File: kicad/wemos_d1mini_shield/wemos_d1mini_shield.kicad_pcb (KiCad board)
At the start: 2 copper layers, 29 parts, among them U1 WeMosD1Mini, U11 74LS125

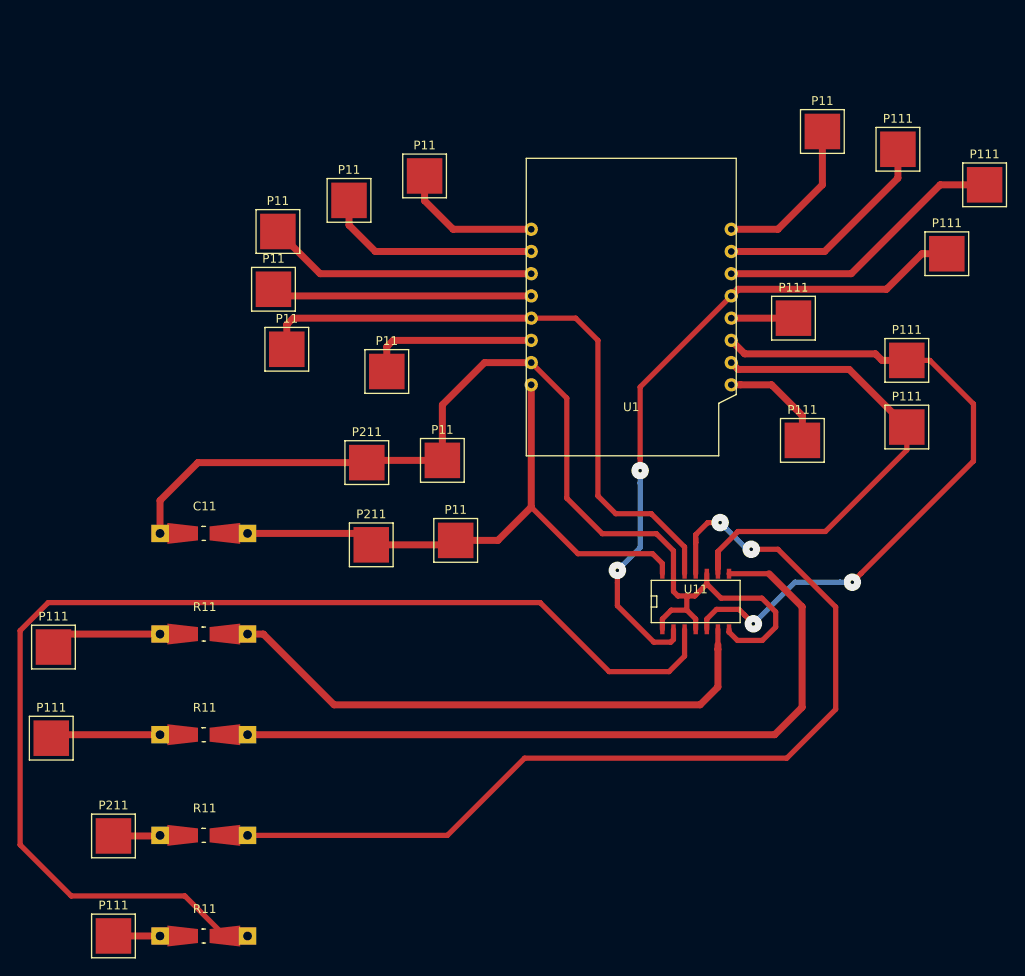
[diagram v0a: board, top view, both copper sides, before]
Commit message: kicad: simplify schematic and begin of routage (WIP)
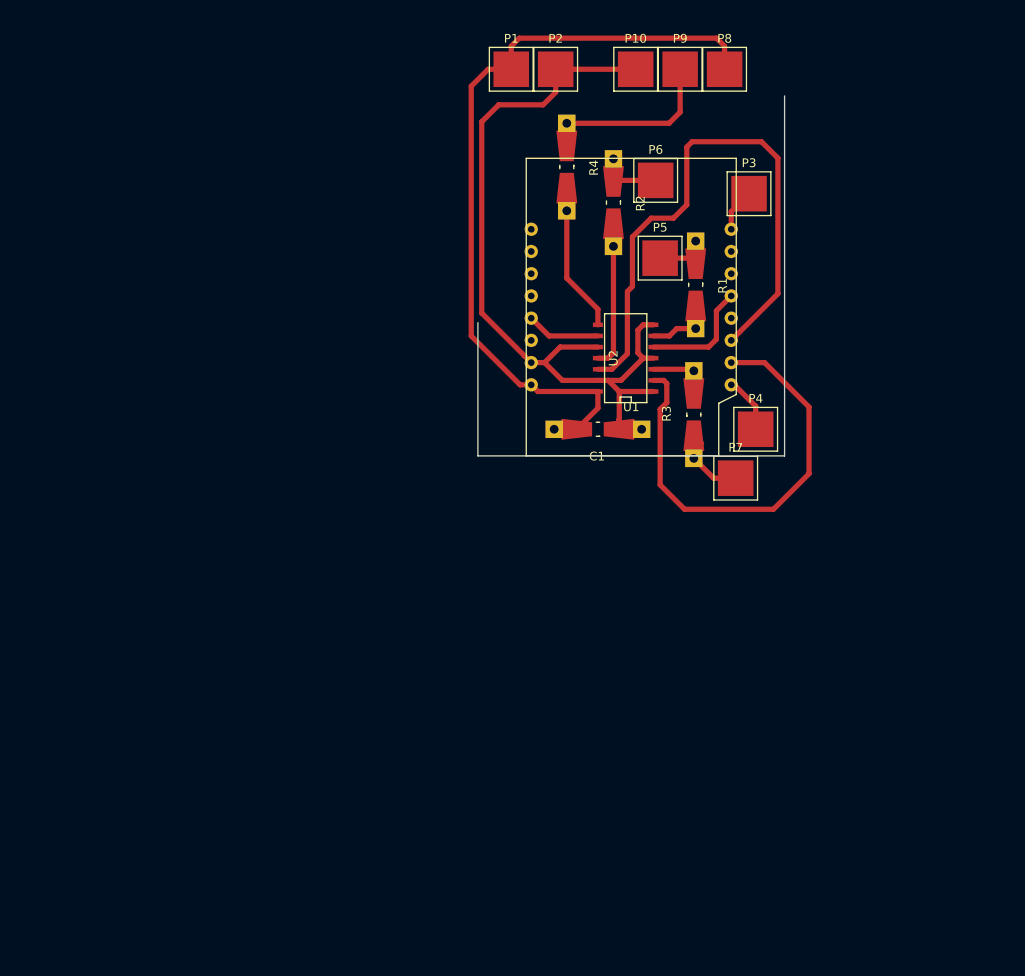
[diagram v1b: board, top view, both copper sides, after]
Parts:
- removed C11: C, Resistors_Universal:Resistor_SMD+THTuniversal_0805to1206_RM10_HandSoldering
- removed P11 (x9), P111 (x10), P211 (x3): ~, SMD_Packages:1Pin
- removed R11 (x4): R, Resistors_Universal:Resistor_SMD+THTuniversal_0805to1206_RM10_HandSoldering
- removed U11: 74LS125, SMD_Packages:SOIC-14_N
- added C1: C, Resistors_Universal:Resistor_SMD+THTuniversal_0805to1206_RM10_HandSoldering, F.Cu at (144.8, 111.8)
- added P1: ~, SMD_Packages:1Pin, F.Cu at (134.9, 70.6)
- added P10: ~, SMD_Packages:1Pin, F.Cu at (149.1, 70.6)
- added P2: ~, SMD_Packages:1Pin, F.Cu at (140.0, 70.6)
- added P3: ~, SMD_Packages:1Pin, F.Cu at (162.1, 84.8)
- added P4: ~, SMD_Packages:1Pin, F.Cu at (162.8, 111.8)
- added P5: ~, SMD_Packages:1Pin, F.Cu at (151.9, 92.2)
- added P6: ~, SMD_Packages:1Pin, F.Cu at (151.4, 83.3)
- added P7: ~, SMD_Packages:1Pin, F.Cu at (160.5, 117.3)
- added P8: ~, SMD_Packages:1Pin, F.Cu at (159.3, 70.6)
- added P9: ~, SMD_Packages:1Pin, F.Cu at (154.2, 70.6)
- added R1: R, Resistors_Universal:Resistor_SMD+THTuniversal_0805to1206_RM10_HandSoldering, F.Cu at (156.0, 95.2)
- added R2: R, Resistors_Universal:Resistor_SMD+THTuniversal_0805to1206_RM10_HandSoldering, F.Cu at (146.6, 85.9)
- added R3: R, Resistors_Universal:Resistor_SMD+THTuniversal_0805to1206_RM10_HandSoldering, F.Cu at (155.7, 110.1)
- added R4: R, Resistors_Universal:Resistor_SMD+THTuniversal_0805to1206_RM10_HandSoldering, F.Cu at (141.2, 81.8)
- added U2: 74LS125, SMD_Packages:SOIC-14_N, F.Cu at (147.8, 103.6)
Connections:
- U1 pad 1: Net-(P3-Pad1) (its old number) -> (no net)
- U1 pad 12: Net-(P12-Pad1) -> (no net)
- U1 pad 14: Net-(P11-Pad1) -> (no net)
- U1 pad 15: Net-(P10-Pad1) -> (no net)
- U1 pad 2: Net-(P4-Pad1) (its old number) -> (no net)
- U1 pad 3: Net-(P5-Pad1) -> (no net)
- U1 pad 4: Net-(P6-Pad1) -> (no net)
- U1 pad 6: Net-(P8-Pad1) -> (no net)
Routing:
- net Net-(R1-Pad2): track 139.1 -> 7.76 mm
- net Net-(R4-Pad2): track 114.8 -> 17.1 mm, vias 2 -> 0
- net Net-(R3-Pad2): track 88.7 -> 7.28 mm
- net Net-(U1-Pad5): track 72.9 -> 8.46 mm
- net Net-(U1-Pad13): track 76.9 -> 13.2 mm, vias 2 -> 0
- net Net-(R2-Pad2): track 67.7 -> 16.8 mm
- net GND: track 127.5 -> 92.3 mm
- net Net-(P11-Pad1): track 33.2 -> 0.00 mm
- net Net-(P10-Pad1): track 25.8 -> 0.00 mm
- net Net-(P4-Pad1) (its old number): track 24.9 -> 0.00 mm
- net Net-(P5-Pad1): track 31.0 -> 6.92 mm
- net Net-(P6-Pad1): track 29.8 -> 7.47 mm
- net Net-(P9-Pad1): track 0.00 -> 21.0 mm
- net Net-(P8-Pad1): track 19.6 -> 0.00 mm
- net VCC: track 70.1 -> 89.3 mm
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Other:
- board outline added: 35.1 x 41.1 mm

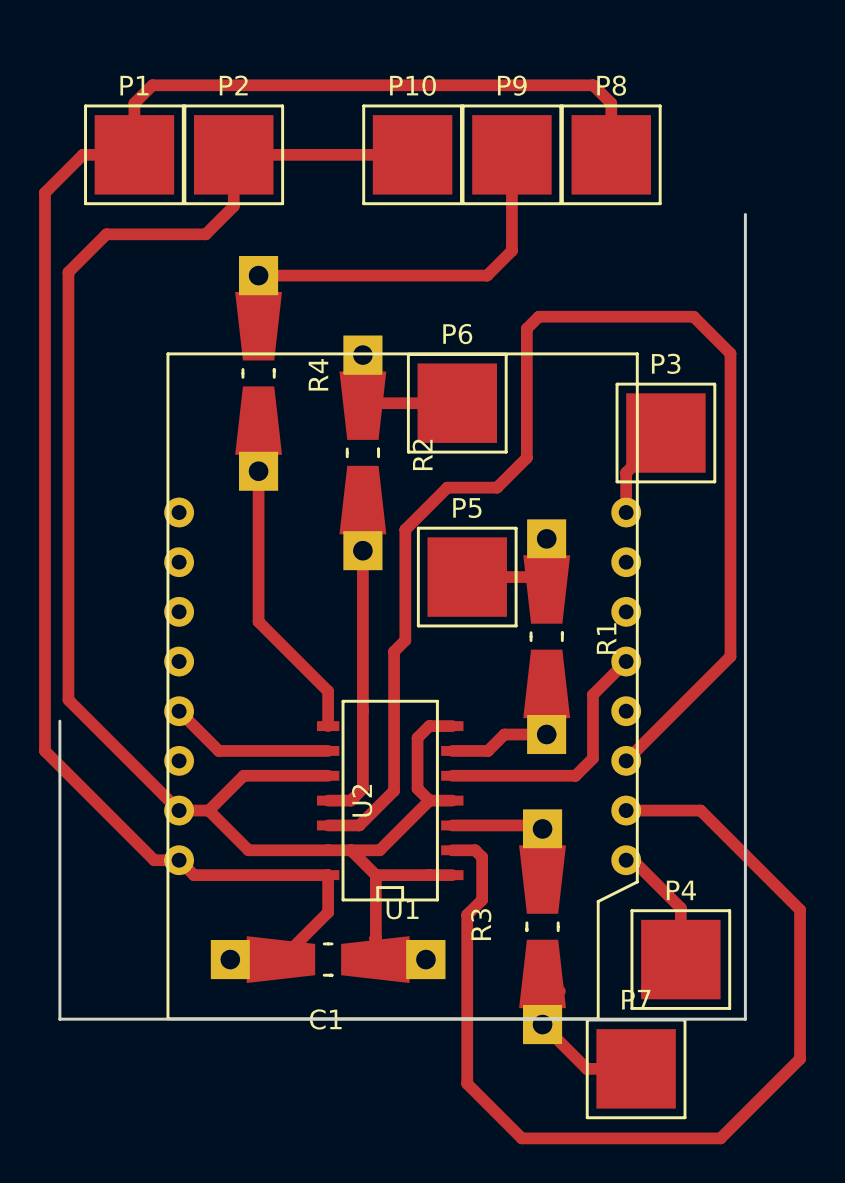
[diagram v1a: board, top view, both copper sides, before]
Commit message: Update PCB design
This design is working and have been used for "BienVenus sur Venus".
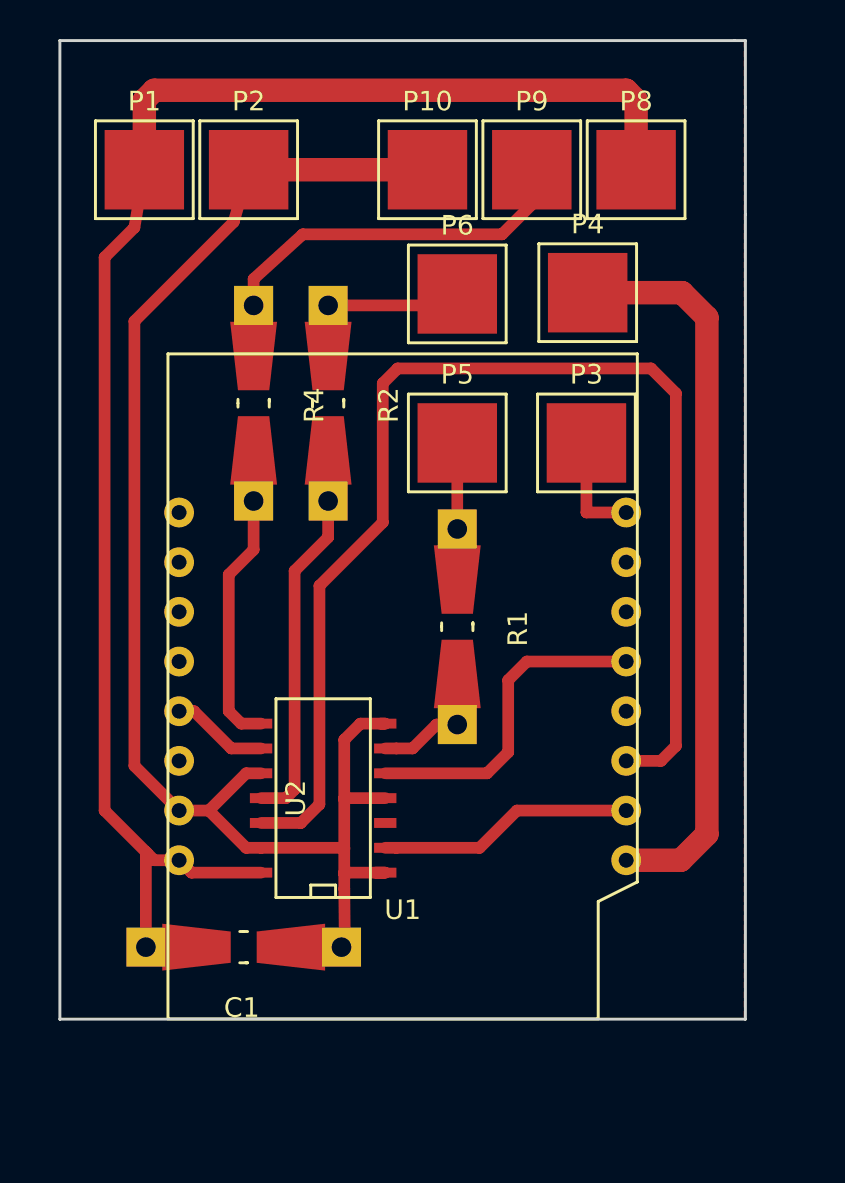
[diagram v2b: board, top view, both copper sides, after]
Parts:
- removed P7: ~, SMD_Packages:1Pin
- removed R3: R, Resistors_Universal:Resistor_SMD+THTuniversal_0805to1206_RM10_HandSoldering
- moved P4 34.4 mm to (158.1, 77.7)
- moved P5 6.88 mm to (151.4, 85.3)
- moved P6 5.59 mm to (151.4, 77.7)
- moved R1 4.60 mm to (151.4, 94.7)
- moved C1 4.36 mm to (140.5, 111.1)
- moved P3 4.10 mm to (158.0, 85.3)
- moved U2 3.43 mm to (144.4, 103.5)
- moved R2 3.10 mm to (144.8, 83.3)
- moved R4 1.55 mm to (141.0, 83.3)
- moved P8 1.48 mm to (160.5, 71.4)
- moved P9 1.27 mm to (155.2, 71.4)
- moved P10 1.08 mm to (149.9, 71.4)
- moved P2 1.08 mm to (140.7, 71.4)
- moved P1 0.92 mm to (135.4, 71.4)
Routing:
- net Net-(U1-Pad10): track 52.4 -> 13.5 mm
- net Net-(P4-Pad1): track 6.09 -> 37.7 mm
- net GND: track 92.3 -> 78.6 mm
- net Net-(P7-Pad1): track 12.2 -> 0.00 mm
- net Net-(R3-Pad2): track 7.28 -> 0.00 mm
- net VCC: track 89.3 -> 84.3 mm
- net Net-(U1-Pad13): track 13.2 -> 16.8 mm
- net Net-(U1-Pad11): track 66.5 -> 63.0 mm
- net Net-(U1-Pad5): track 8.46 -> 4.98 mm
- net Net-(R2-Pad2): track 16.8 -> 19.9 mm
- net Net-(R4-Pad2): track 17.1 -> 15.9 mm
- net Net-(R1-Pad2): track 7.76 -> 6.78 mm
- net Net-(P6-Pad1): track 7.47 -> 8.39 mm
- net Net-(P3-Pad1): track 4.91 -> 5.59 mm
- added copper zone on F.Cu, net GND
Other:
- board size 35.1 x 41.1 mm -> 35.1 x 50 mm
- net class LED power added: clearance 0.6, trace_width 1.2, via_dia 2, via_drill 0.4
